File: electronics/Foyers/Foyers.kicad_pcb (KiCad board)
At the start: 2 copper layers, 32 x 34.5 mm, 11 parts, among them J1 RJ45, J2 2601-1102, J3 2601-1104

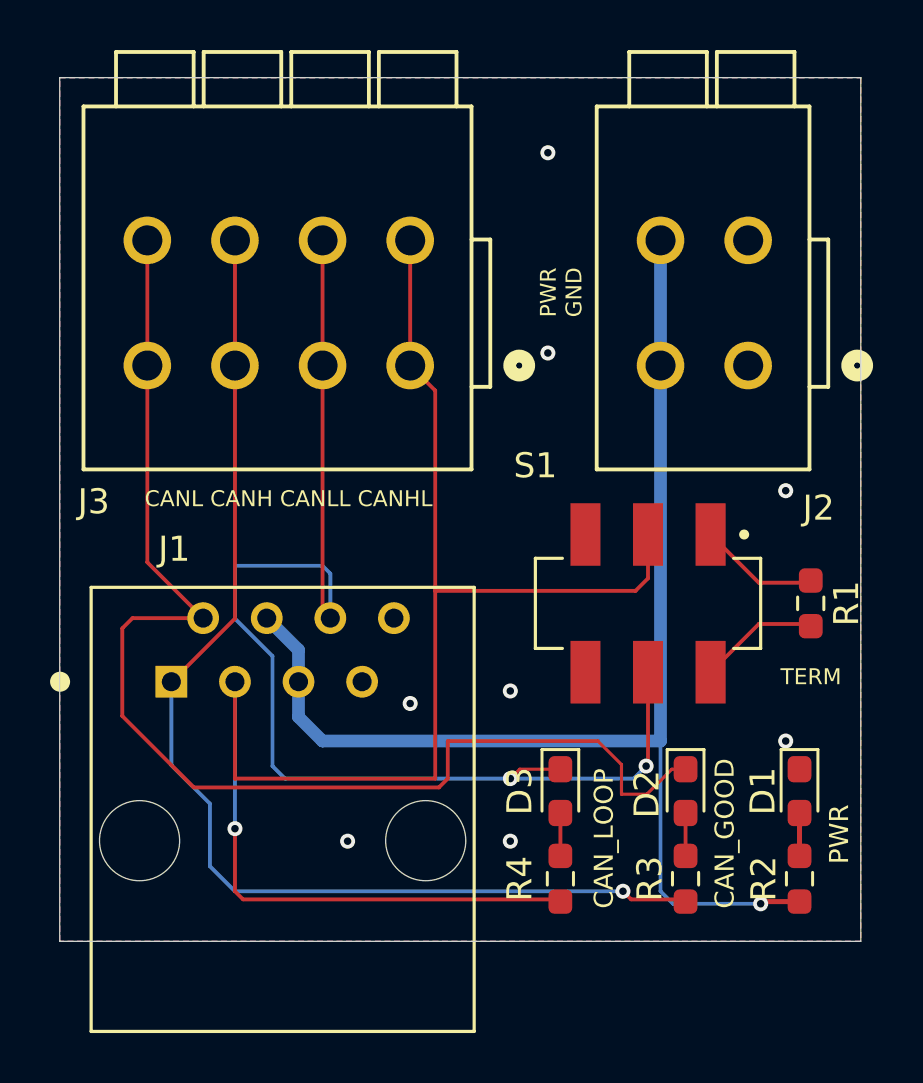
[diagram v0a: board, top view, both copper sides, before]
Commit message: Pulling Rev B into main (#1)
* Planning on ordering more back porches.
* Various updates to the footprints. Added datasheets.
* Added the software.
* Verified CAN, voltage input, current reading although the resistor is off, and temperature reading.
* Many updates to get things dialed in. Have the ABS signal working. But there is a small glitch to it.
* Inc encoder is now working as well.
* Added a bootloader.

* Bootloader is working to the point it can push new images into app code space.

* Refactored the CAN messages. Programming is working, at least pushing code. Build version strings are working correctly.

* Refactored the CAN messages. Programming is working, at least pushing code. Build version strings are working correctly.

* Bootblock will reboot on watchdog and stay in the bootblock.

* Forgot to add the auto increment version.

* Updated the bootblock functionality. I am able to program an app code image now.

* I can now reprogram app code from app code.

* Bootloading is working well.

* Updated the README file. It still needs some work.

* The bootblock now allows me to reprogram the bootblock.

* Many refactors to support different deviceIDs. Currently app code can't write to FLASH.

* This is mostly working.

* Things are working well. I can reprogram different units. The CAN status LED flashes as heartbeat messages come in.

* In the app added CAN bus utilization, sorted by device ID. Changed to the release build for the backporch, changed task names, moved can TX tasks into one thread and CAN Rx tasks into a second thread. Fixed a bug with the bootloader picking up the wrong device ID.

* Added the wpilib code. I have only tested the Java code and it works.
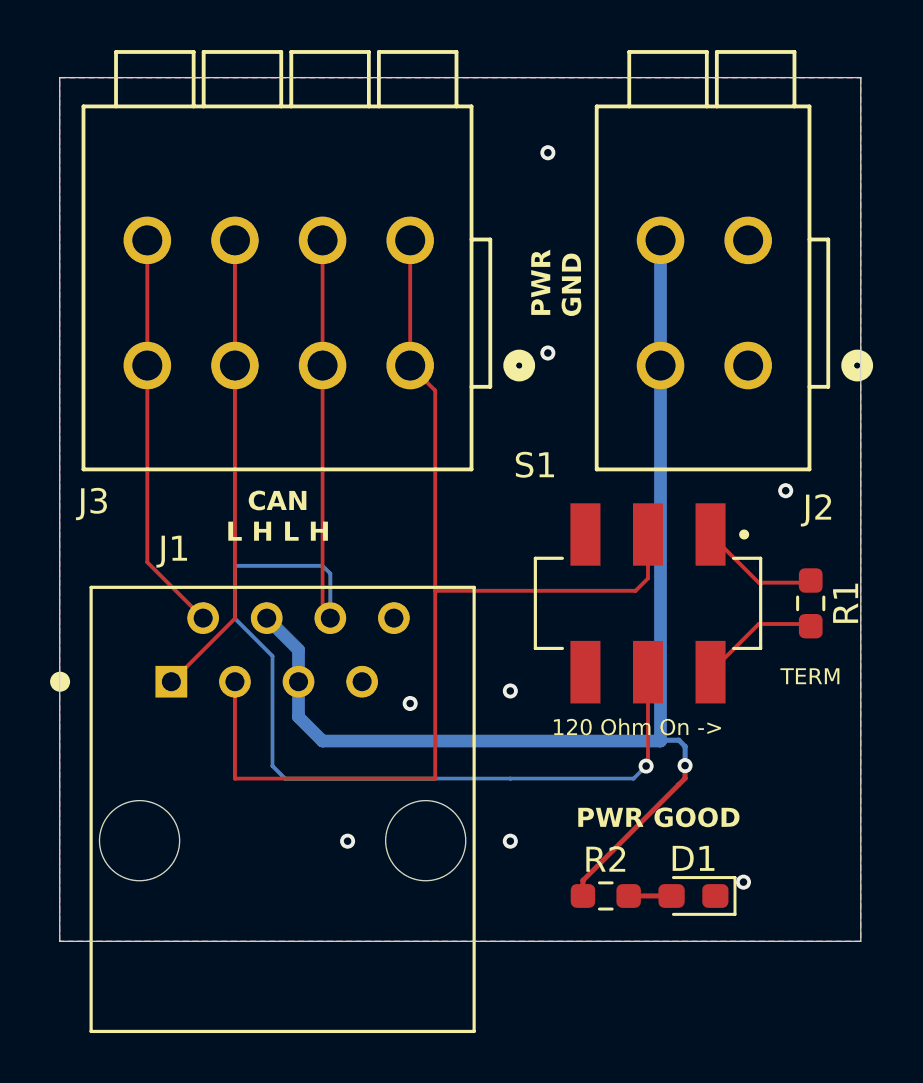
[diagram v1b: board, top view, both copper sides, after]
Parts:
- removed D2, D3: LED, LED_SMD:LED_0603_1608Metric_Pad1.05x0.95mm_HandSolder
- removed R3, R4: 680, Resistor_SMD:R_0603_1608Metric_Pad0.98x0.95mm_HandSolder
- moved R2 7.77 mm to (154.3, 107.2), turned to 0 degrees
- moved D1 5.96 mm to (157.8, 107.2), turned to 180 degrees
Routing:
- net /CAN_LOW: track 50.2 -> 16.0 mm
- net /CAN_HIGH: track 46.2 -> 18.7 mm, vias 1 -> 0
- net /CAN_HIGH_LOOP: track 65.7 -> 44.2 mm, vias 1 -> 0
- net /VBAT: track 51.4 -> 48.1 mm
- net /CAN_LOW_LOOP: track 50.8 -> 48.7 mm, vias 2 -> 1
- net Net-(D3-A): track 1.86 -> 0.00 mm
- net Net-(D2-A): track 1.86 -> 0.00 mm
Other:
- board text added: "120 Ohm On ->"
- board text added: "CAN L H L H"
- board text added: "FOYER REV B Team 7048/4360 2026"
- board text added: "PWR GOOD"
- board text removed: "CANL CANH CANLL CANHL"
- board text removed: "CAN_GOOD"
- board text removed: "CAN_LOOP"
- board text removed: "FOYER REV A Team 7048/4360"
- board text removed: "PWR"
